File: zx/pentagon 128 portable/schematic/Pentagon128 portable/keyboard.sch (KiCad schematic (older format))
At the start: 34 parts

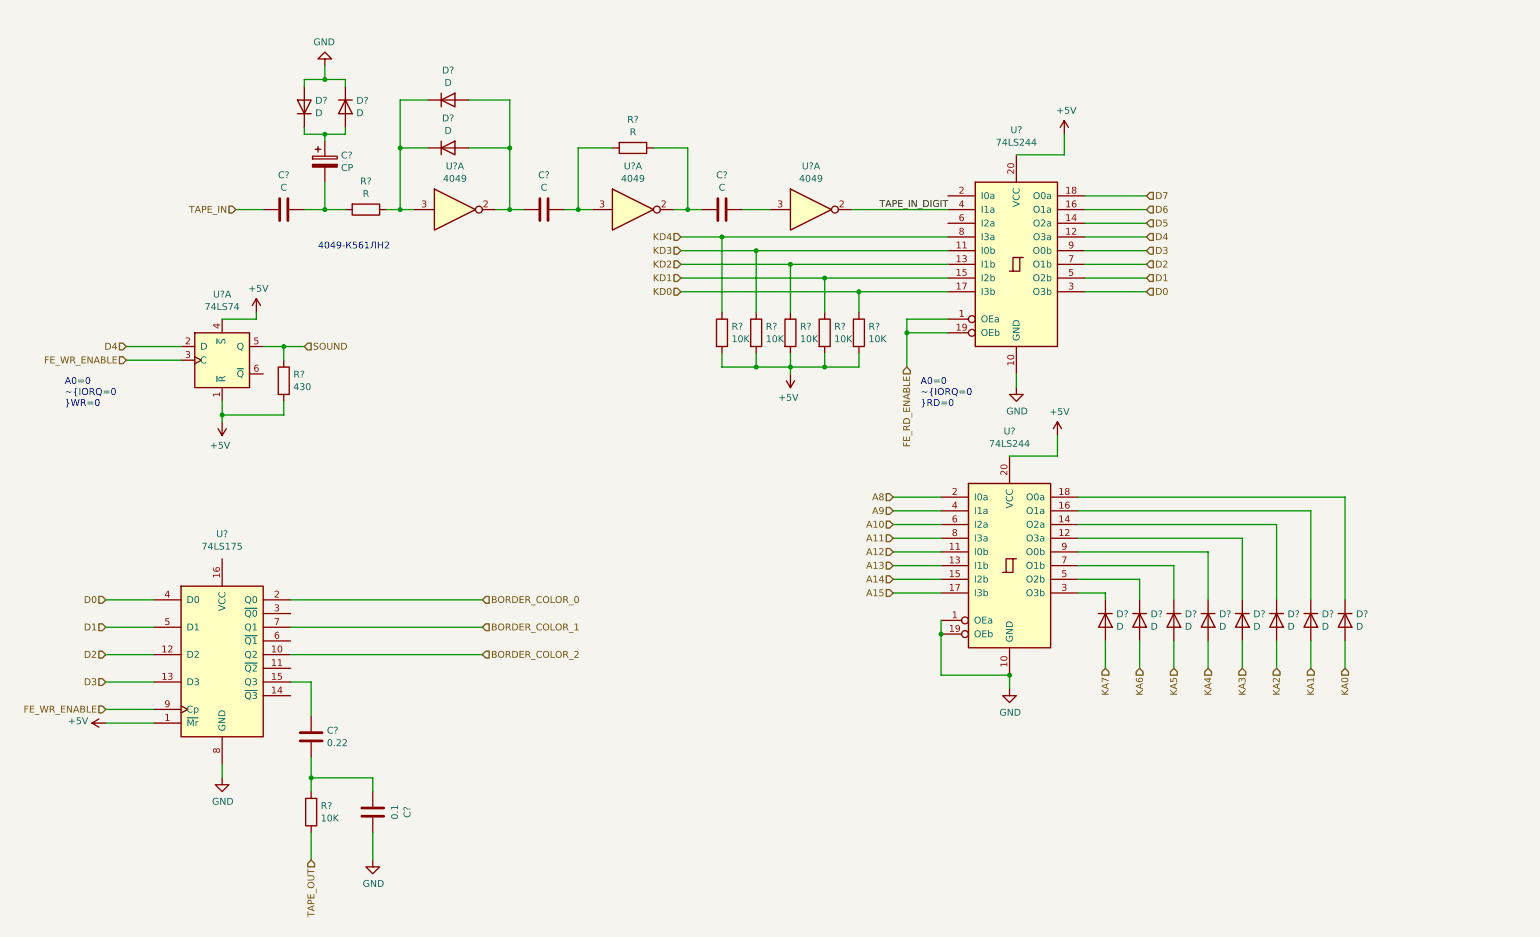
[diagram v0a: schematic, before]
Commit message: reorganizing. finished ram and keyboard, updated z80
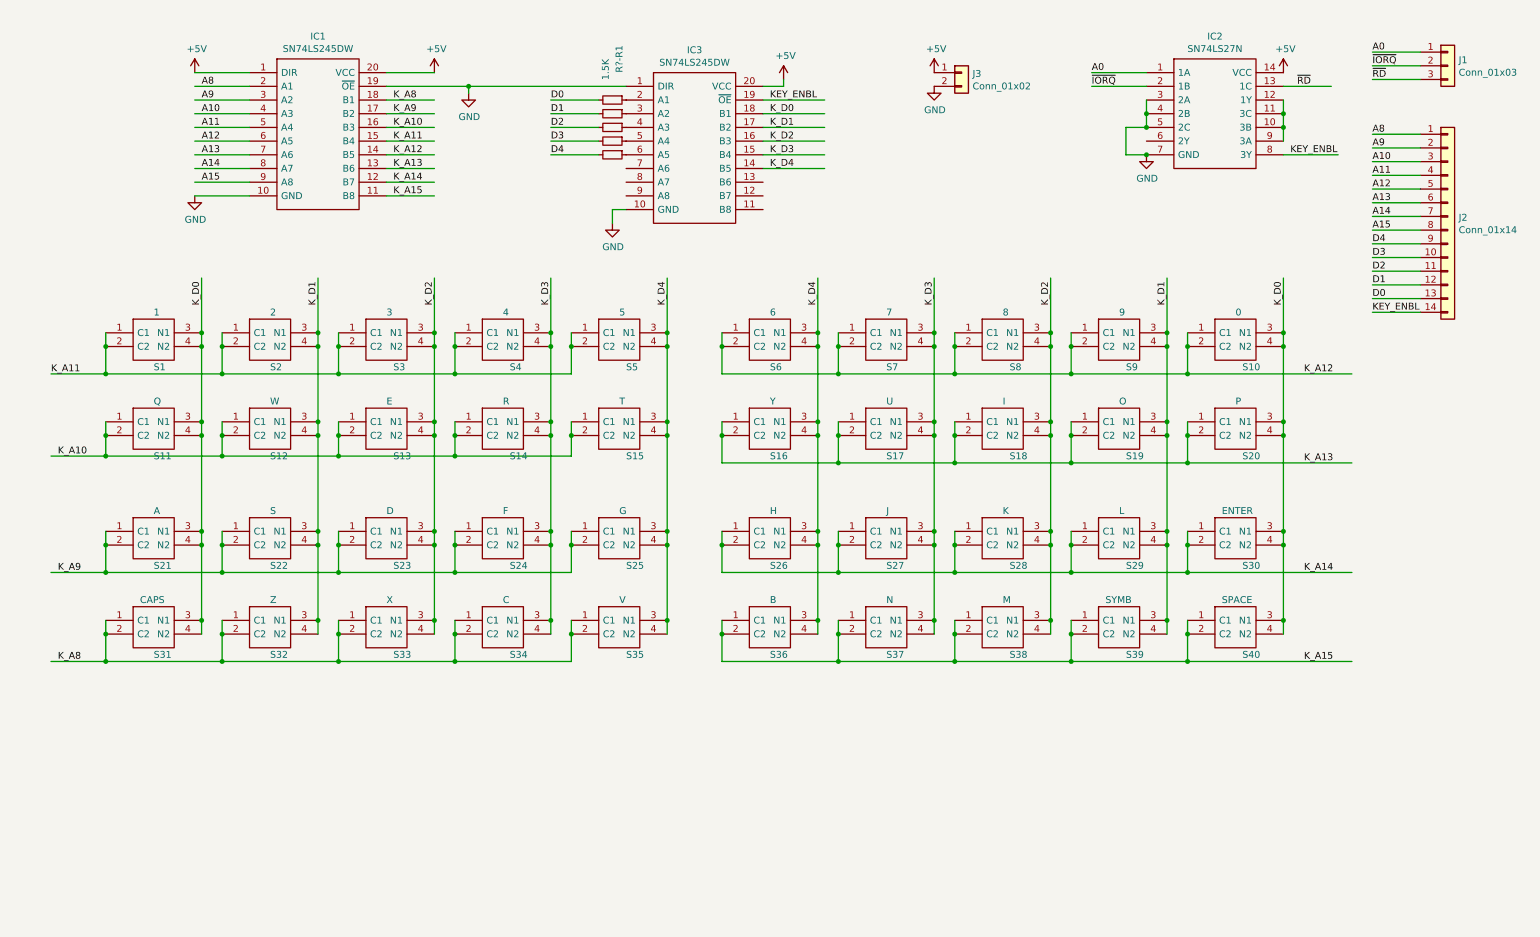
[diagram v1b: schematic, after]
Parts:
- removed C? (x3): C, symbol Device:C
- removed C?: CP, symbol Device:CP
- removed C?: 0.22, symbol Device:C
- removed C?: 0.1, symbol Device:C
- removed D? (x12): D, symbol Device:D
- removed R? (x6): 10K, symbol Device:R
- removed R? (x2): R, symbol Device:R
- removed R?: 430, symbol Device:R
- removed U? (x2): 74LS244, symbol 74xx:74LS244
- removed U? (x3): 4049, symbol 4xxx:4049
- removed U?: 74LS74, symbol 74xx:74LS74
- removed U?: 74LS175, symbol 74xx:74LS175
- added IC1, IC3: SN74LS245DW, SamacSys_Parts:SOIC127P1030X265-20N, symbol SamacSys_Parts:SN74LS245DW
- added IC2: SN74LS27N, SamacSys_Parts:DIP794W53P254L1930H508Q14N, symbol SamacSys_Parts:SN74LS27N
- added J1: Conn_01x03, Connector_PinHeader_2.54mm:PinHeader_1x03_P2.54mm_Vertical, symbol Connector_Generic:Conn_01x03
- added J2: Conn_01x14, Connector_PinHeader_2.54mm:PinHeader_1x14_P2.54mm_Vertical, symbol Connector_Generic:Conn_01x14
- added J3: Conn_01x02, Connector_PinHeader_2.54mm:PinHeader_1x02_P2.54mm_Vertical, symbol Connector_Generic:Conn_01x02
- added R1, R2, R3, R4, R?-R1: 1.5K, Resistor_SMD:R_0402_1005Metric, symbol Device:R_Small
- added S1: 1, SamacSys_Parts:118259104, symbol SamacSys_Parts:1-1825910-4
- added S10: 0, SamacSys_Parts:118259104, symbol SamacSys_Parts:1-1825910-4
- added S11: Q, SamacSys_Parts:118259104, symbol SamacSys_Parts:1-1825910-4
- added S12: W, SamacSys_Parts:118259104, symbol SamacSys_Parts:1-1825910-4
- added S13: E, SamacSys_Parts:118259104, symbol SamacSys_Parts:1-1825910-4
- added S14: R, SamacSys_Parts:118259104, symbol SamacSys_Parts:1-1825910-4
- added S15: T, SamacSys_Parts:118259104, symbol SamacSys_Parts:1-1825910-4
- added S16: Y, SamacSys_Parts:118259104, symbol SamacSys_Parts:1-1825910-4
- added S17: U, SamacSys_Parts:118259104, symbol SamacSys_Parts:1-1825910-4
- added S18: I, SamacSys_Parts:118259104, symbol SamacSys_Parts:1-1825910-4
- added S19: O, SamacSys_Parts:118259104, symbol SamacSys_Parts:1-1825910-4
- added S2: 2, SamacSys_Parts:118259104, symbol SamacSys_Parts:1-1825910-4
- added S20: P, SamacSys_Parts:118259104, symbol SamacSys_Parts:1-1825910-4
- added S21: A, SamacSys_Parts:118259104, symbol SamacSys_Parts:1-1825910-4
- added S22: S, SamacSys_Parts:118259104, symbol SamacSys_Parts:1-1825910-4
- added S23: D, SamacSys_Parts:118259104, symbol SamacSys_Parts:1-1825910-4
- added S24: F, SamacSys_Parts:118259104, symbol SamacSys_Parts:1-1825910-4
- added S25: G, SamacSys_Parts:118259104, symbol SamacSys_Parts:1-1825910-4
- added S26: H, SamacSys_Parts:118259104, symbol SamacSys_Parts:1-1825910-4
- added S27: J, SamacSys_Parts:118259104, symbol SamacSys_Parts:1-1825910-4
- added S28: K, SamacSys_Parts:118259104, symbol SamacSys_Parts:1-1825910-4
- added S29: L, SamacSys_Parts:118259104, symbol SamacSys_Parts:1-1825910-4
- added S3: 3, SamacSys_Parts:118259104, symbol SamacSys_Parts:1-1825910-4
- added S30: ENTER, SamacSys_Parts:118259104, symbol SamacSys_Parts:1-1825910-4
- added S31: CAPS, SamacSys_Parts:118259104, symbol SamacSys_Parts:1-1825910-4
- added S32: Z, SamacSys_Parts:118259104, symbol SamacSys_Parts:1-1825910-4
- added S33: X, SamacSys_Parts:118259104, symbol SamacSys_Parts:1-1825910-4
- added S34: C, SamacSys_Parts:118259104, symbol SamacSys_Parts:1-1825910-4
- added S35: V, SamacSys_Parts:118259104, symbol SamacSys_Parts:1-1825910-4
- added S36: B, SamacSys_Parts:118259104, symbol SamacSys_Parts:1-1825910-4
- added S37: N, SamacSys_Parts:118259104, symbol SamacSys_Parts:1-1825910-4
- added S38: M, SamacSys_Parts:118259104, symbol SamacSys_Parts:1-1825910-4
- added S39: SYMB, SamacSys_Parts:118259104, symbol SamacSys_Parts:1-1825910-4
- added S4: 4, SamacSys_Parts:118259104, symbol SamacSys_Parts:1-1825910-4
- added S40: SPACE, SamacSys_Parts:118259104, symbol SamacSys_Parts:1-1825910-4
- added S5: 5, SamacSys_Parts:118259104, symbol SamacSys_Parts:1-1825910-4
- added S6: 6, SamacSys_Parts:118259104, symbol SamacSys_Parts:1-1825910-4
- added S7: 7, SamacSys_Parts:118259104, symbol SamacSys_Parts:1-1825910-4
- added S8: 8, SamacSys_Parts:118259104, symbol SamacSys_Parts:1-1825910-4
- added S9: 9, SamacSys_Parts:118259104, symbol SamacSys_Parts:1-1825910-4
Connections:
- net labels added: A0, KEY_ENBL, K_A10, K_A11, K_A12, K_A13, K_A14, K_A15, K_A8, K_A9, K_D0, K_D1, K_D2, K_D3, K_D4, ~IORQ, ~RD
- net labels removed: BORDER_COLOR_0, BORDER_COLOR_1, BORDER_COLOR_2, D5, D6, D7, FE_RD_ENABLE, FE_WR_ENABLE, KA0, KA1, KA2, KA3, KA4, KA5, KA6, KA7, KD0, KD1, KD2, KD3, KD4, SOUND, TAPE_IN, TAPE_IN_DIGIT, TAPE_OUT
- wire segments 143 -> 266
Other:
- note removed: "4049-К561ЛН2"
- note removed: "A0=0\n~IORQ=0\n~RD=0"
- note removed: "A0=0\n~IORQ=0\n~WR=0"

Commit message: updated ram 128k, 512k, keyboard
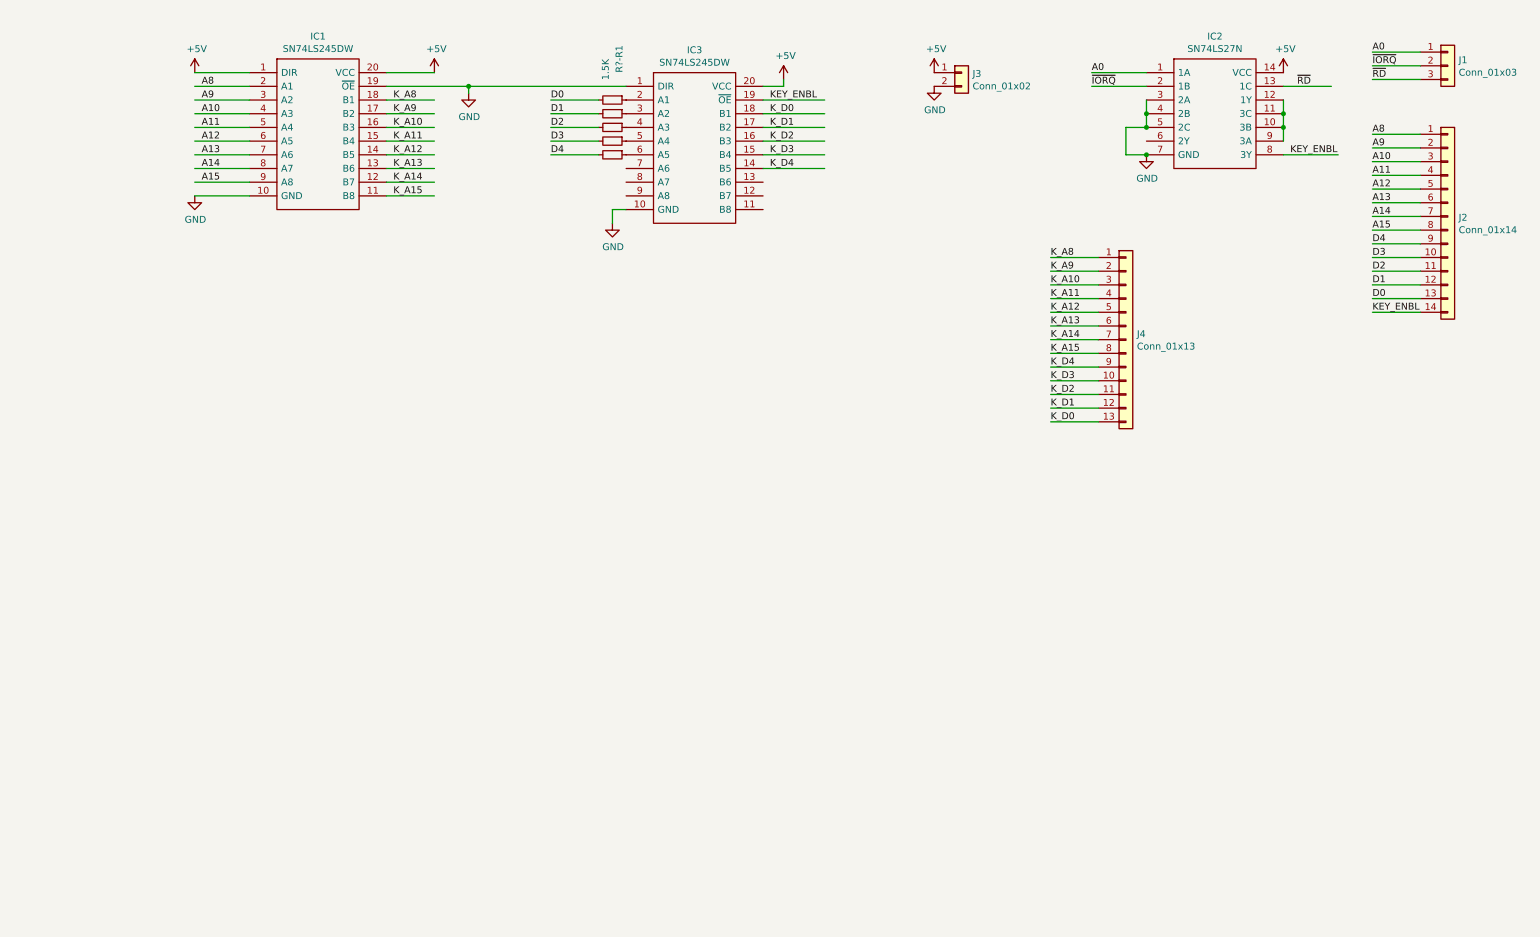
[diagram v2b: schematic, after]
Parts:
- removed S1: 1, SamacSys_Parts:118259104, symbol SamacSys_Parts:1-1825910-4
- removed S10: 0, SamacSys_Parts:118259104, symbol SamacSys_Parts:1-1825910-4
- removed S11: Q, SamacSys_Parts:118259104, symbol SamacSys_Parts:1-1825910-4
- removed S12: W, SamacSys_Parts:118259104, symbol SamacSys_Parts:1-1825910-4
- removed S13: E, SamacSys_Parts:118259104, symbol SamacSys_Parts:1-1825910-4
- removed S14: R, SamacSys_Parts:118259104, symbol SamacSys_Parts:1-1825910-4
- removed S15: T, SamacSys_Parts:118259104, symbol SamacSys_Parts:1-1825910-4
- removed S16: Y, SamacSys_Parts:118259104, symbol SamacSys_Parts:1-1825910-4
- removed S17: U, SamacSys_Parts:118259104, symbol SamacSys_Parts:1-1825910-4
- removed S18: I, SamacSys_Parts:118259104, symbol SamacSys_Parts:1-1825910-4
- removed S19: O, SamacSys_Parts:118259104, symbol SamacSys_Parts:1-1825910-4
- removed S2: 2, SamacSys_Parts:118259104, symbol SamacSys_Parts:1-1825910-4
- removed S20: P, SamacSys_Parts:118259104, symbol SamacSys_Parts:1-1825910-4
- removed S21: A, SamacSys_Parts:118259104, symbol SamacSys_Parts:1-1825910-4
- removed S22: S, SamacSys_Parts:118259104, symbol SamacSys_Parts:1-1825910-4
- removed S23: D, SamacSys_Parts:118259104, symbol SamacSys_Parts:1-1825910-4
- removed S24: F, SamacSys_Parts:118259104, symbol SamacSys_Parts:1-1825910-4
- removed S25: G, SamacSys_Parts:118259104, symbol SamacSys_Parts:1-1825910-4
- removed S26: H, SamacSys_Parts:118259104, symbol SamacSys_Parts:1-1825910-4
- removed S27: J, SamacSys_Parts:118259104, symbol SamacSys_Parts:1-1825910-4
- removed S28: K, SamacSys_Parts:118259104, symbol SamacSys_Parts:1-1825910-4
- removed S29: L, SamacSys_Parts:118259104, symbol SamacSys_Parts:1-1825910-4
- removed S3: 3, SamacSys_Parts:118259104, symbol SamacSys_Parts:1-1825910-4
- removed S30: ENTER, SamacSys_Parts:118259104, symbol SamacSys_Parts:1-1825910-4
- removed S31: CAPS, SamacSys_Parts:118259104, symbol SamacSys_Parts:1-1825910-4
- removed S32: Z, SamacSys_Parts:118259104, symbol SamacSys_Parts:1-1825910-4
- removed S33: X, SamacSys_Parts:118259104, symbol SamacSys_Parts:1-1825910-4
- removed S34: C, SamacSys_Parts:118259104, symbol SamacSys_Parts:1-1825910-4
- removed S35: V, SamacSys_Parts:118259104, symbol SamacSys_Parts:1-1825910-4
- removed S36: B, SamacSys_Parts:118259104, symbol SamacSys_Parts:1-1825910-4
- removed S37: N, SamacSys_Parts:118259104, symbol SamacSys_Parts:1-1825910-4
- removed S38: M, SamacSys_Parts:118259104, symbol SamacSys_Parts:1-1825910-4
- removed S39: SYMB, SamacSys_Parts:118259104, symbol SamacSys_Parts:1-1825910-4
- removed S4: 4, SamacSys_Parts:118259104, symbol SamacSys_Parts:1-1825910-4
- removed S40: SPACE, SamacSys_Parts:118259104, symbol SamacSys_Parts:1-1825910-4
- removed S5: 5, SamacSys_Parts:118259104, symbol SamacSys_Parts:1-1825910-4
- removed S6: 6, SamacSys_Parts:118259104, symbol SamacSys_Parts:1-1825910-4
- removed S7: 7, SamacSys_Parts:118259104, symbol SamacSys_Parts:1-1825910-4
- removed S8: 8, SamacSys_Parts:118259104, symbol SamacSys_Parts:1-1825910-4
- removed S9: 9, SamacSys_Parts:118259104, symbol SamacSys_Parts:1-1825910-4
- added J4: Conn_01x13, Connector_PinSocket_2.54mm:PinSocket_1x13_P2.54mm_Vertical, symbol Connector_Generic:Conn_01x13
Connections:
- wire segments 266 -> 79

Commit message: some reordering in the main project
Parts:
- removed J1: Conn_01x03, Connector_PinHeader_2.54mm:PinHeader_1x03_P2.54mm_Vertical, symbol Connector_Generic:Conn_01x03
- removed J2: Conn_01x14, Connector_PinHeader_2.54mm:PinHeader_1x14_P2.54mm_Vertical, symbol Connector_Generic:Conn_01x14
- removed J3: Conn_01x02, Connector_PinHeader_2.54mm:PinHeader_1x02_P2.54mm_Vertical, symbol Connector_Generic:Conn_01x02
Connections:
- wire segments 79 -> 62
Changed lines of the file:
@@
 $Descr A4 11693 8268
 encoding utf-8
-Sheet 1 1
+Sheet 8 14
 Title ""
 Date ""
@@
 Text Label 9800 1550 0    50   ~ 0
 KEY_ENBL
-$Comp
-L Connector_Generic:Conn_01x03 J1
-U 1 1 5F648B45
-P 10950 900
-F 0 "J1" H 11030 942 50  0000 L CNN
-F 1 "Conn_01x03" H 11030 851 50  0000 L CNN
-F 2 "Connector_PinHeader_2.54mm:PinHeader_1x03_P2.54mm_Vertical" H 10950 900 50  0001 C CNN
-F 3 "~" H 10950 900 50  0001 C CNN
-	1    10950 900
-	1    0    0    -1
-$EndComp
-Wire Wire Line
-	10750 800  10400 800
-Wire Wire Line
-	10750 900  10400 900
-Wire Wire Line
-	10750 1000 10400 1000
-Text Label 10400 800  0    50   ~ 0
-A0
-Text Label 10400 1000 0    50   ~ 0
-~RD
-Text Label 10400 900  0    50   ~ 0
-~IORQ
-$Comp
-L Connector_Generic:Conn_01x14 J2
-U 1 1 5F68D465
-P 10950 2000
-F 0 "J2" H 11030 1992 50  0000 L CNN
-F 1 "Conn_01x14" H 11030 1901 50  0000 L CNN
-F 2 "Connector_PinHeader_2.54mm:PinHeader_1x14_P2.54mm_Vertical" H 10950 2000 50  0001 C CNN
-F 3 "~" H 10950 2000 50  0001 C CNN
-	1    10950 2000
-	1    0    0    -1
-$EndComp
-Wire Wire Line
-	10750 1400 10400 1400
-Wire Wire Line
-	10750 1500 10400 1500
-Wire Wire Line
-	10750 1600 10400 1600
-Wire Wire Line
-	10750 1700 10400 1700
-Wire Wire Line
-	10750 1800 10400 1800
-Wire Wire Line
-	10750 1900 10400 1900
-Wire Wire Line
-	10750 2000 10400 2000
-Wire Wire Line
-	10750 2100 10400 2100
-Wire Wire Line
-	10750 2200 10400 2200
-Wire Wire Line
-	10750 2300 10400 2300
-Wire Wire Line
-	10750 2400 10400 2400
-Wire Wire Line
-	10750 2500 10400 2500
-Wire Wire Line
-	10750 2600 10400 2600
-Wire Wire Line
-	10750 2700 10400 2700
-Text Label 10400 2700 0    50   ~ 0
-KEY_ENBL
-Text Label 10400 1400 0    50   ~ 0
-A8
-Text Label 10400 1500 0    50   ~ 0
-A9
-Text Label 10400 1600 0    50   ~ 0
-A10
-Text Label 10400 1700 0    50   ~ 0
-A11
-Text Label 10400 1800 0    50   ~ 0
-A12
-Text Label 10400 1900 0    50   ~ 0
-A13
-Text Label 10400 2000 0    50   ~ 0
-A14
-Text Label 10400 2100 0    50   ~ 0
-A15
-Text Label 10400 2600 0    50   ~ 0
-D0
-Text Label 10400 2500 0    50   ~ 0
-D1
-Text Label 10400 2400 0    50   ~ 0
-D2
-Text Label 10400 2300 0    50   ~ 0
-D3
-Text Label 10400 2200 0    50   ~ 0
-D4
-$Comp
-L Connector_Generic:Conn_01x02 J3
-U 1 1 5F885BE0
-P 7400 950
-F 0 "J3" H 7480 942 50  0000 L CNN
-F 1 "Conn_01x02" H 7480 851 50  0000 L CNN
-F 2 "Connector_PinHeader_2.54mm:PinHeader_1x02_P2.54mm_Vertical" H 7400 950 50  0001 C CNN
-F 3 "~" H 7400 950 50  0001 C CNN
-	1    7400 950
-	1    0    0    -1
-$EndComp
-$Comp
-L power:+5V #PWR0109
-U 1 1 5F8866E2
-P 7200 950
-F 0 "#PWR0109" H 7200 800 50  0001 C CNN
-F 1 "+5V" H 7215 1123 50  0000 C CNN
-F 2 "" H 7200 950 50  0001 C CNN
-F 3 "" H 7200 950 50  0001 C CNN
-	1    7200 950
-	1    0    0    -1
-$EndComp
-$Comp
-L power:GND #PWR0110
-U 1 1 5F886BFC
-P 7200 1050
-F 0 "#PWR0110" H 7200 800 50  0001 C CNN
-F 1 "GND" H 7205 877 50  0000 C CNN
-F 2 "" H 7200 1050 50  0001 C CNN
-F 3 "" H 7200 1050 50  0001 C CNN
-	1    7200 1050
-	1    0    0    -1
-$EndComp
 Wire Wire Line
 	8750 1150 8750 1250
@@
 Text Label 8050 3100 0    50   ~ 0
 K_D4
+Text HLabel 8350 950  0    50   Input ~ 0
+A0
+Text HLabel 8350 1050 0    50   Input ~ 0
+~IORQ
+Text HLabel 10100 1050 2    50   Input ~ 0
+~RD
+Text HLabel 4400 1150 0    50   Input ~ 0
+D0
+Text HLabel 4400 1250 0    50   Input ~ 0
+D1
+Text HLabel 4400 1350 0    50   Input ~ 0
+D2
+Text HLabel 4400 1450 0    50   Input ~ 0
+D3
+Text HLabel 4400 1550 0    50   Input ~ 0
+D4
+Text HLabel 1800 1050 0    50   Input ~ 0
+A8
+Text HLabel 1800 1150 0    50   Input ~ 0
+A9
+Text HLabel 1800 1250 0    50   Input ~ 0
+A10
+Text HLabel 1800 1350 0    50   Input ~ 0
+A11
+Text HLabel 1800 1450 0    50   Input ~ 0
+A12
+Text HLabel 1800 1550 0    50   Input ~ 0
+A13
+Text HLabel 1800 1650 0    50   Input ~ 0
+A14
+Text HLabel 1800 1750 0    50   Input ~ 0
+A15
 $EndSCHEMATC
